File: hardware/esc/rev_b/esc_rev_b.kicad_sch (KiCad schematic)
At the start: 0 parts

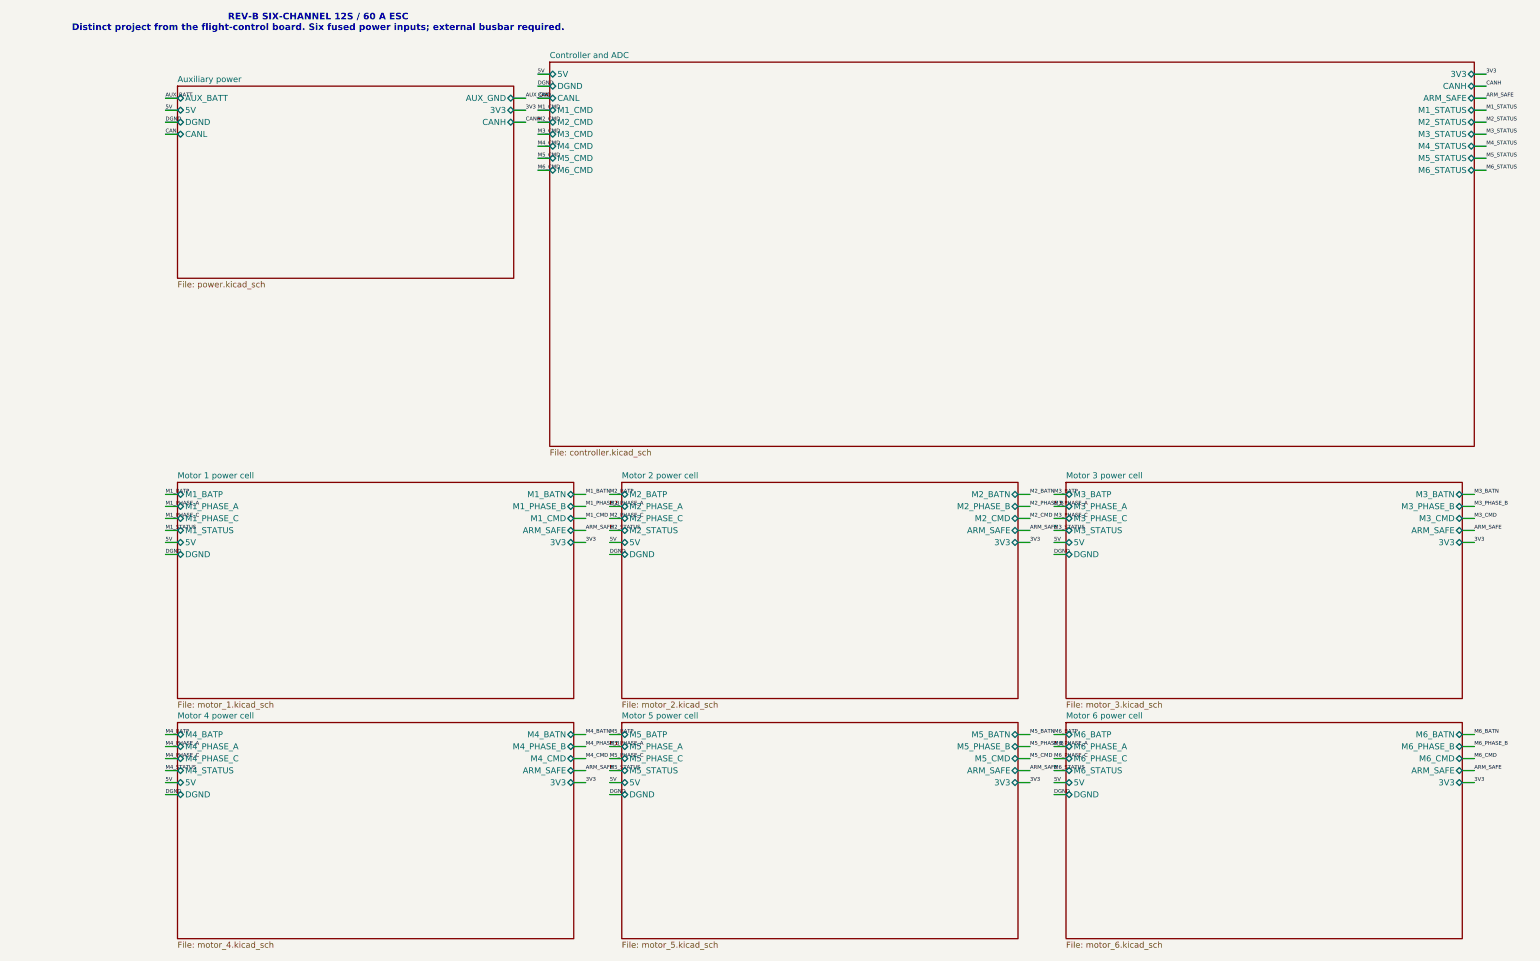
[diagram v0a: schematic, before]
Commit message: Add ESC USB-C programming interfaces
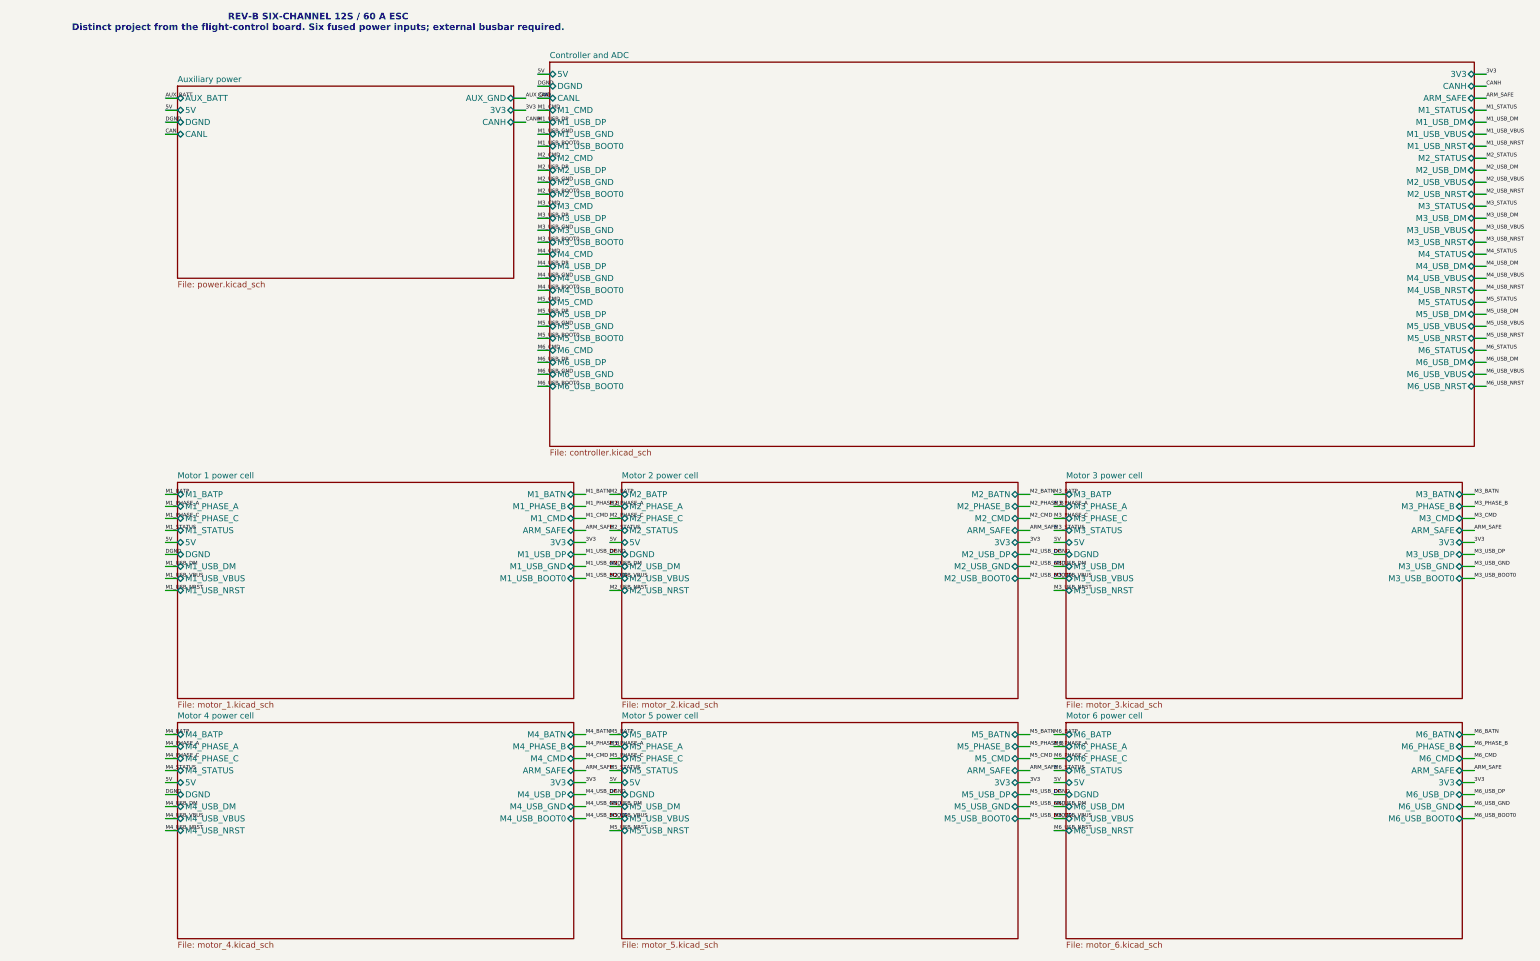
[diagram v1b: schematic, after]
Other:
- sheet Controller and ADC ports: added M1_USB_BOOT0, M1_USB_DM, M1_USB_DP, M1_USB_GND, M1_USB_NRST, M1_USB_VBUS, M2_USB_BOOT0, M2_USB_DM, M2_USB_DP, M2_USB_GND, M2_USB_NRST, M2_USB_VBUS, M3_USB_BOOT0, M3_USB_DM, M3_USB_DP, M3_USB_GND, M3_USB_NRST, M3_USB_VBUS, M4_USB_BOOT0, M4_USB_DM, M4_USB_DP, M4_USB_GND, M4_USB_NRST, M4_USB_VBUS, M5_USB_BOOT0, M5_USB_DM, M5_USB_DP, M5_USB_GND, M5_USB_NRST, M5_USB_VBUS, M6_USB_BOOT0, M6_USB_DM, M6_USB_DP, M6_USB_GND, M6_USB_NRST, M6_USB_VBUS; removed none
- sheet Motor 1 power cell ports: added M1_USB_BOOT0, M1_USB_DM, M1_USB_DP, M1_USB_GND, M1_USB_NRST, M1_USB_VBUS; removed none
- sheet Motor 2 power cell ports: added M2_USB_BOOT0, M2_USB_DM, M2_USB_DP, M2_USB_GND, M2_USB_NRST, M2_USB_VBUS; removed none
- sheet Motor 3 power cell ports: added M3_USB_BOOT0, M3_USB_DM, M3_USB_DP, M3_USB_GND, M3_USB_NRST, M3_USB_VBUS; removed none
- sheet Motor 4 power cell ports: added M4_USB_BOOT0, M4_USB_DM, M4_USB_DP, M4_USB_GND, M4_USB_NRST, M4_USB_VBUS; removed none
- sheet Motor 5 power cell ports: added M5_USB_BOOT0, M5_USB_DM, M5_USB_DP, M5_USB_GND, M5_USB_NRST, M5_USB_VBUS; removed none
- sheet Motor 6 power cell ports: added M6_USB_BOOT0, M6_USB_DM, M6_USB_DP, M6_USB_GND, M6_USB_NRST, M6_USB_VBUS; removed none

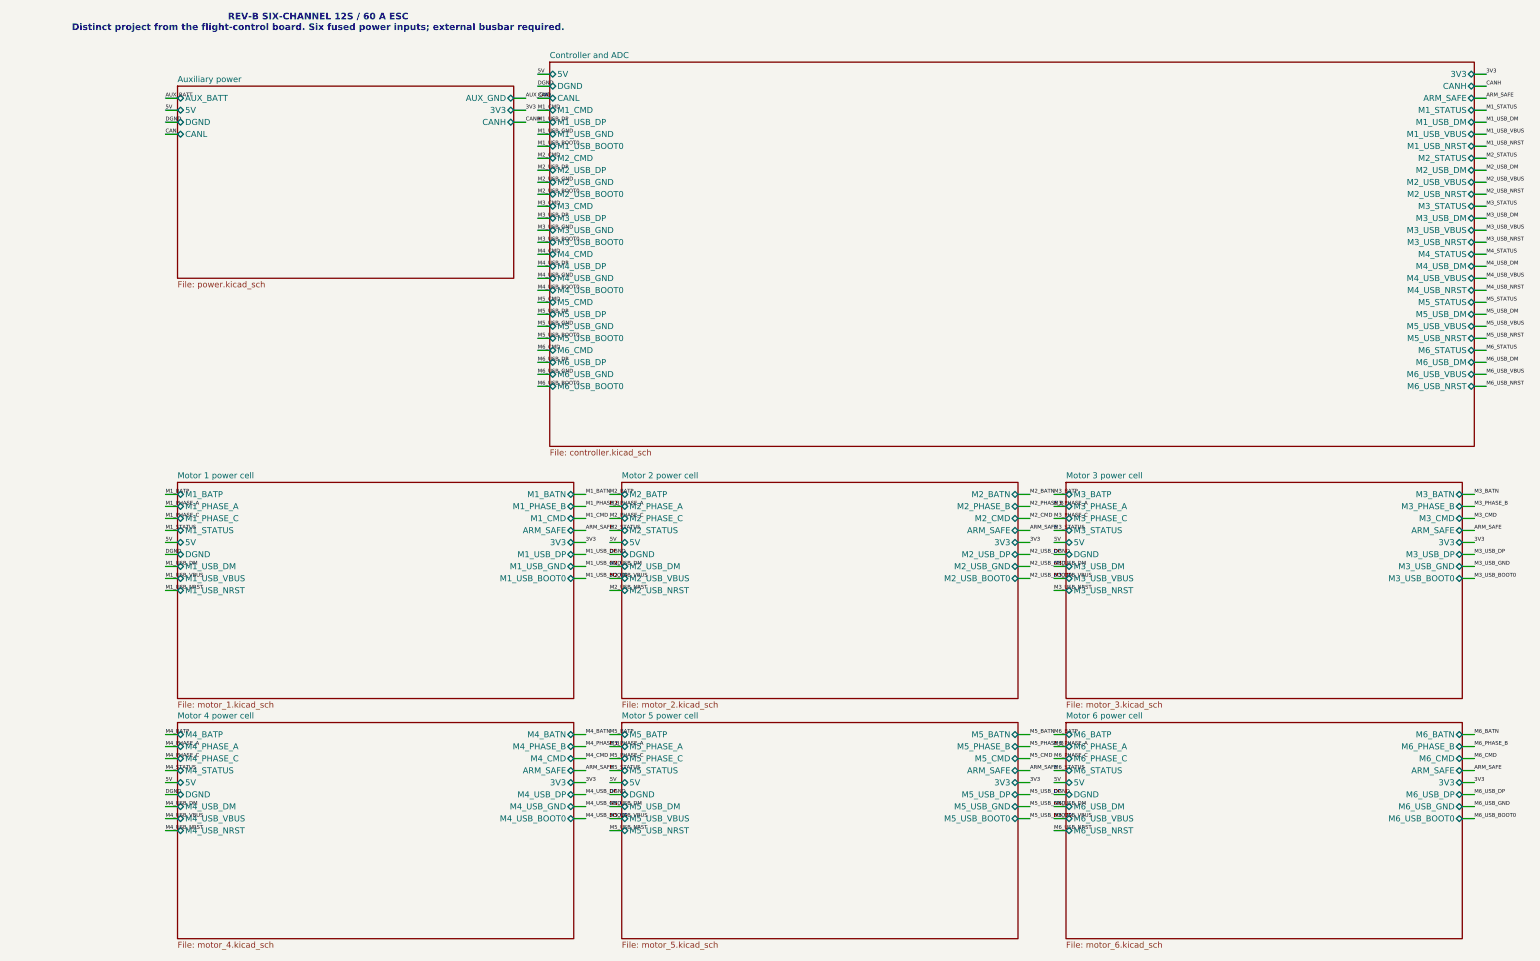
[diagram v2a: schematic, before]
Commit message: Replace ESC selector with seven-pin active-low control
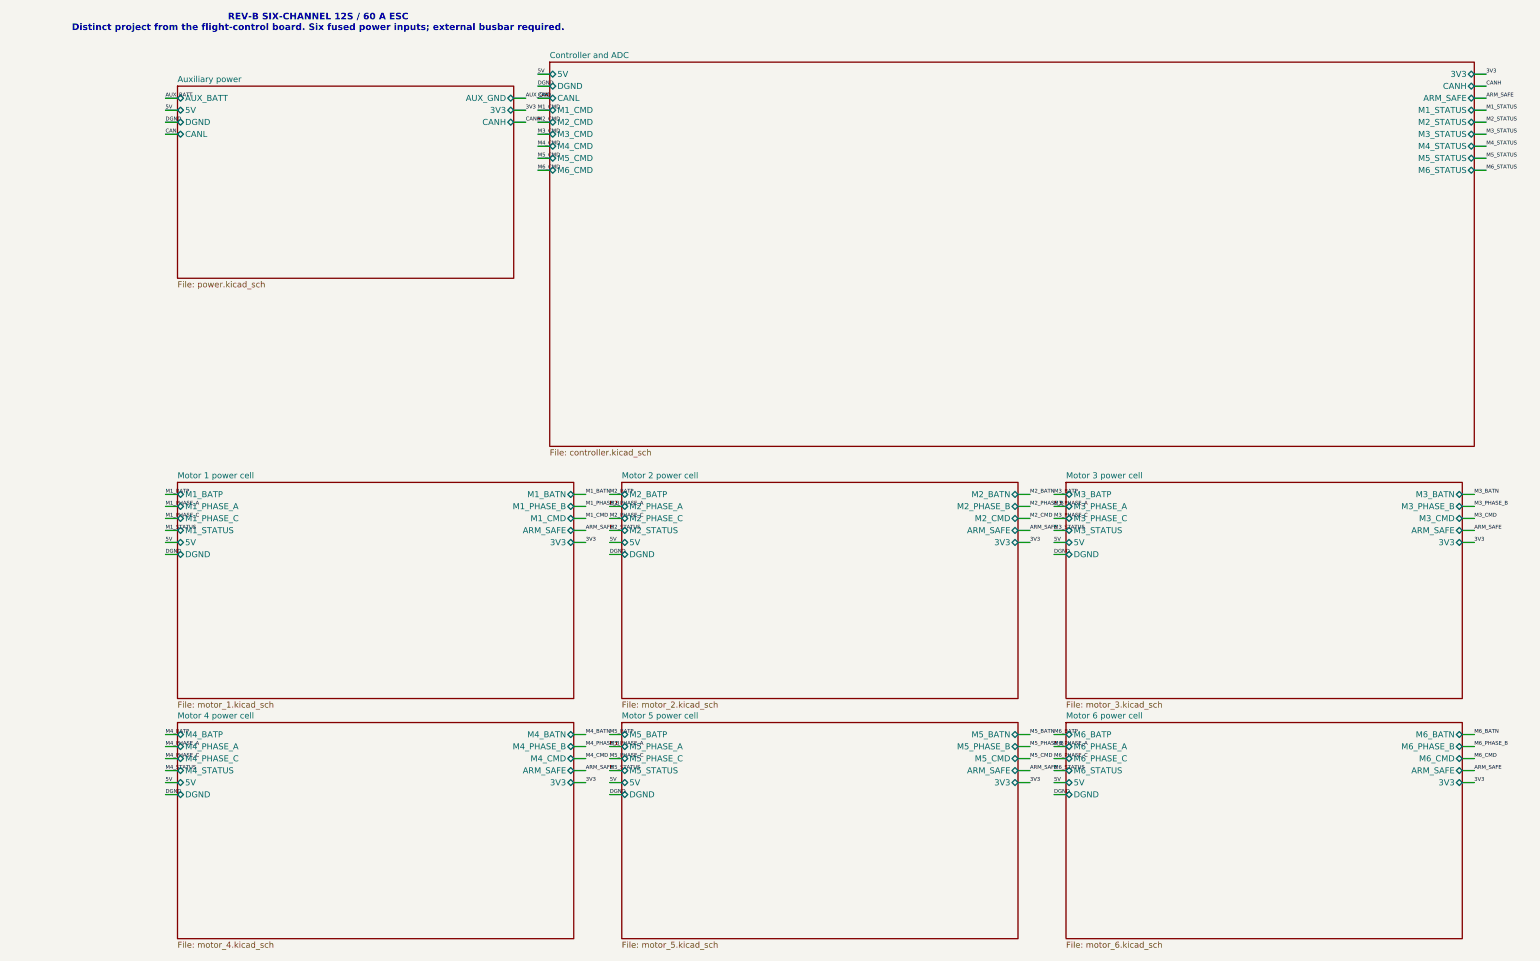
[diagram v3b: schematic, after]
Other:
- sheet Controller and ADC ports: added none; removed M1_USB_BOOT0, M1_USB_DM, M1_USB_DP, M1_USB_GND, M1_USB_NRST, M1_USB_VBUS, M2_USB_BOOT0, M2_USB_DM, M2_USB_DP, M2_USB_GND, M2_USB_NRST, M2_USB_VBUS, M3_USB_BOOT0, M3_USB_DM, M3_USB_DP, M3_USB_GND, M3_USB_NRST, M3_USB_VBUS, M4_USB_BOOT0, M4_USB_DM, M4_USB_DP, M4_USB_GND, M4_USB_NRST, M4_USB_VBUS, M5_USB_BOOT0, M5_USB_DM, M5_USB_DP, M5_USB_GND, M5_USB_NRST, M5_USB_VBUS, M6_USB_BOOT0, M6_USB_DM, M6_USB_DP, M6_USB_GND, M6_USB_NRST, M6_USB_VBUS
- sheet Motor 1 power cell ports: added none; removed M1_USB_BOOT0, M1_USB_DM, M1_USB_DP, M1_USB_GND, M1_USB_NRST, M1_USB_VBUS
- sheet Motor 2 power cell ports: added none; removed M2_USB_BOOT0, M2_USB_DM, M2_USB_DP, M2_USB_GND, M2_USB_NRST, M2_USB_VBUS
- sheet Motor 3 power cell ports: added none; removed M3_USB_BOOT0, M3_USB_DM, M3_USB_DP, M3_USB_GND, M3_USB_NRST, M3_USB_VBUS
- sheet Motor 4 power cell ports: added none; removed M4_USB_BOOT0, M4_USB_DM, M4_USB_DP, M4_USB_GND, M4_USB_NRST, M4_USB_VBUS
- sheet Motor 5 power cell ports: added none; removed M5_USB_BOOT0, M5_USB_DM, M5_USB_DP, M5_USB_GND, M5_USB_NRST, M5_USB_VBUS
- sheet Motor 6 power cell ports: added none; removed M6_USB_BOOT0, M6_USB_DM, M6_USB_DP, M6_USB_GND, M6_USB_NRST, M6_USB_VBUS
